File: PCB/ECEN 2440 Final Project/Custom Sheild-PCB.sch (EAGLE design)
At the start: 4 parts

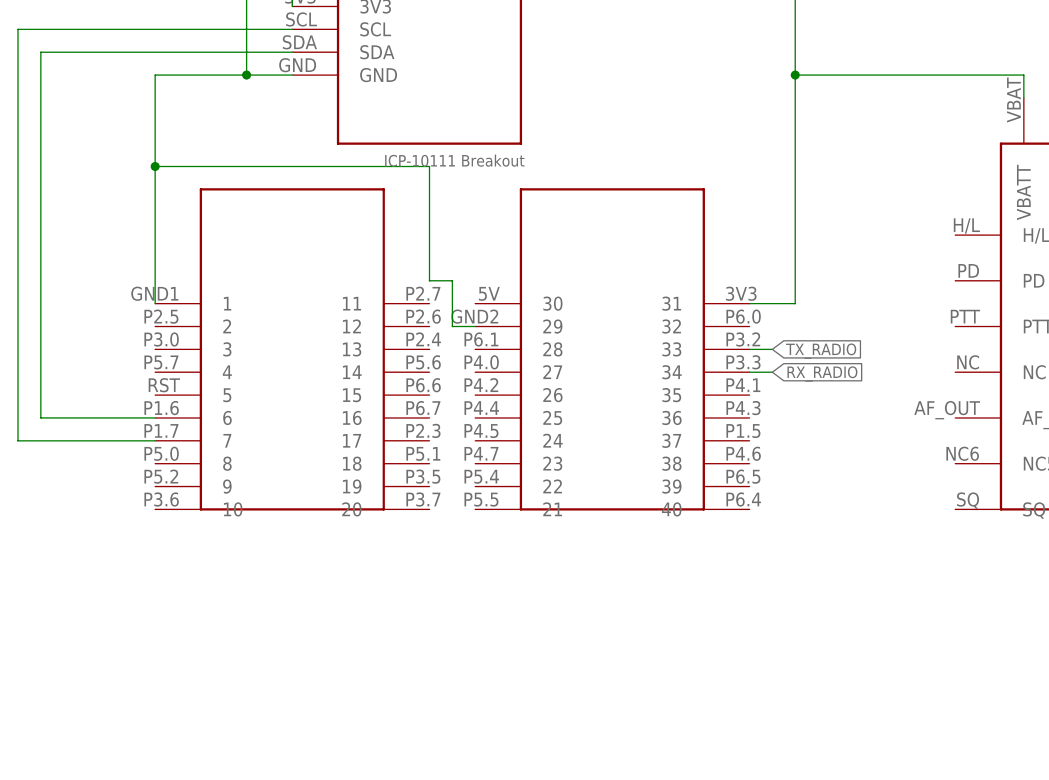
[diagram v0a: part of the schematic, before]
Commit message: made a couple connections
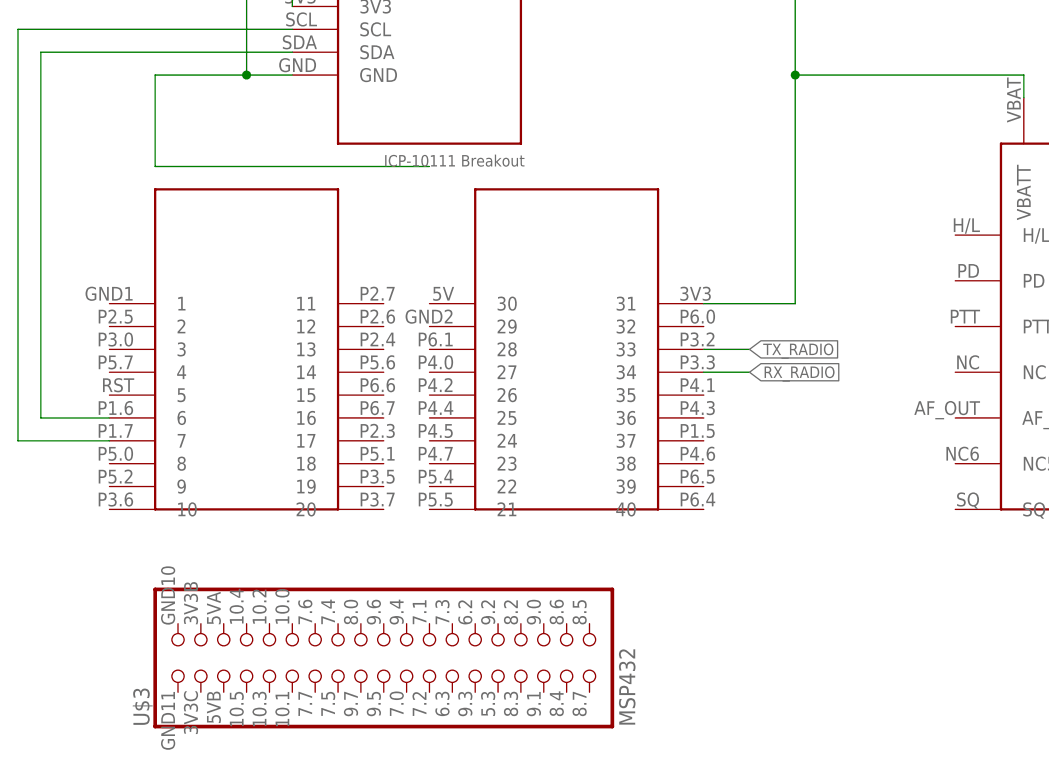
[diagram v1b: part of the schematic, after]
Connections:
- net GND1: no longer U$3.1, U$3.29
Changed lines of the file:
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@@
 <part name="U$1" library="adafruit" library_urn="urn:adsk.eagle:library:420" deviceset="MICROSD" device="" package3d_urn="urn:adsk.eagle:package:6240723/1"/>
 <part name="U$2" library="Custom Library" deviceset="ALTIMETER" device=""/>
+<part name="U$4" library="Custom Library" deviceset="RADIO" device=""/>
 <part name="U$3" library="Custom Library" deviceset="MSP432" device=""/>
-<part name="U$4" library="Custom Library" deviceset="RADIO" device=""/>
 </parts>
 <sheets>
@@
 <attribute name="NAME" x="76.2" y="60.96" size="1.27" layer="95" rot="R180"/>
 </instance>
-<instance part="U$3" gate="MSP432" x="50.8" y="27.94" smashed="yes"/>
 <instance part="U$4" gate="G$1" x="129.54" y="0" smashed="yes"/>
+<instance part="U$3" gate="MSP432" x="45.72" y="27.94" smashed="yes">
+<attribute name="NAME" x="34.925" y="-24.13" size="1.778" layer="95" rot="R90"/>
+<attribute name="VALUE" x="88.9" y="-24.13" size="1.778" layer="96" rot="R90"/>
+</instance>
 </instances>
 <busses>
@@
 <net name="GND1" class="0">
 <segment>
-<pinref part="U$3" gate="MSP432" pin="1"/>
 <pinref part="U$2" gate="G$1" pin="GND"/>
-<wire x1="35.56" y1="22.86" x2="35.56" y2="38.1" width="0.1524" layer="91"/>
 <wire x1="35.56" y1="38.1" x2="35.56" y2="48.26" width="0.1524" layer="91"/>
 <wire x1="35.56" y1="48.26" x2="45.72" y2="48.26" width="0.1524" layer="91"/>
 <wire x1="45.72" y1="48.26" x2="50.8" y2="48.26" width="0.1524" layer="91"/>
-<junction x="35.56" y="38.1"/>
 <wire x1="66.04" y1="38.1" x2="35.56" y2="38.1" width="0.1524" layer="91"/>
 <wire x1="45.72" y1="73.66" x2="45.72" y2="63.5" width="0.1524" layer="91"/>
@@
 <junction x="142.24" y="45.72"/>
 <junction x="45.72" y="63.5"/>
-<wire x1="66.04" y1="38.1" x2="66.04" y2="25.4" width="0.1524" layer="91"/>
-<wire x1="66.04" y1="25.4" x2="68.58" y2="25.4" width="0.1524" layer="91"/>
-<wire x1="68.58" y1="25.4" x2="68.58" y2="20.32" width="0.1524" layer="91"/>
-<pinref part="U$3" gate="MSP432" pin="29"/>
-<wire x1="68.58" y1="20.32" x2="71.12" y2="20.32" width="0.1524" layer="91"/>
 </segment>
 </net>
 <net name="N$1" class="0">
 <segment>
-<pinref part="U$3" gate="MSP432" pin="6"/>
-<wire x1="35.56" y1="10.16" x2="22.86" y2="10.16" width="0.1524" layer="91"/>
 <pinref part="U$2" gate="G$1" pin="SDA"/>
 <wire x1="22.86" y1="10.16" x2="22.86" y2="50.8" width="0.1524" layer="91"/>
 <wire x1="22.86" y1="50.8" x2="50.8" y2="50.8" width="0.1524" layer="91"/>
+<pinref part="U$3" gate="MSP432" pin="6"/>
+<wire x1="22.86" y1="10.16" x2="30.48" y2="10.16" width="0.1524" layer="91"/>
 </segment>
 </net>
 <net name="N$2" class="0">
 <segment>
-<pinref part="U$3" gate="MSP432" pin="7"/>
-<wire x1="35.56" y1="7.62" x2="20.32" y2="7.62" width="0.1524" layer="91"/>
 <pinref part="U$2" gate="G$1" pin="SCL"/>
 <wire x1="20.32" y1="7.62" x2="20.32" y2="53.34" width="0.1524" layer="91"/>
 <wire x1="20.32" y1="53.34" x2="50.8" y2="53.34" width="0.1524" layer="91"/>
+<pinref part="U$3" gate="MSP432" pin="7"/>
+<wire x1="20.32" y1="7.62" x2="30.48" y2="7.62" width="0.1524" layer="91"/>
 </segment>
 </net>
 <net name="N$3" class="0">
 <segment>
-<pinref part="U$3" gate="MSP432" pin="31"/>
-<wire x1="101.6" y1="22.86" x2="106.68" y2="22.86" width="0.1524" layer="91"/>
 <wire x1="106.68" y1="22.86" x2="106.68" y2="48.26" width="0.1524" layer="91"/>
 <wire x1="106.68" y1="48.26" x2="132.08" y2="48.26" width="0.1524" layer="91"/>
@@
 <wire x1="106.68" y1="60.96" x2="106.68" y2="48.26" width="0.1524" layer="91"/>
 <junction x="106.68" y="48.26"/>
+<pinref part="U$3" gate="MSP432" pin="31"/>
+<wire x1="106.68" y1="22.86" x2="96.52" y2="22.86" width="0.1524" layer="91"/>
 </segment>
 </net>
@@
 <segment>
 <pinref part="U$3" gate="MSP432" pin="34"/>
-<wire x1="101.6" y1="15.24" x2="104.14" y2="15.24" width="0.1524" layer="91"/>
-<label x="104.14" y="15.24" size="1.27" layer="95" xref="yes"/>
+<wire x1="96.52" y1="15.24" x2="101.6" y2="15.24" width="0.1524" layer="91"/>
+<label x="101.6" y="15.24" size="1.27" layer="95" xref="yes"/>
 </segment>
 </net>
@@
 <segment>
 <pinref part="U$3" gate="MSP432" pin="33"/>
-<wire x1="101.6" y1="17.78" x2="104.14" y2="17.78" width="0.1524" layer="91"/>
-<label x="104.14" y="17.78" size="1.27" layer="95" xref="yes"/>
+<wire x1="96.52" y1="17.78" x2="101.6" y2="17.78" width="0.1524" layer="91"/>
+<label x="101.6" y="17.78" size="1.27" layer="95" xref="yes"/>
 </segment>
 </net>

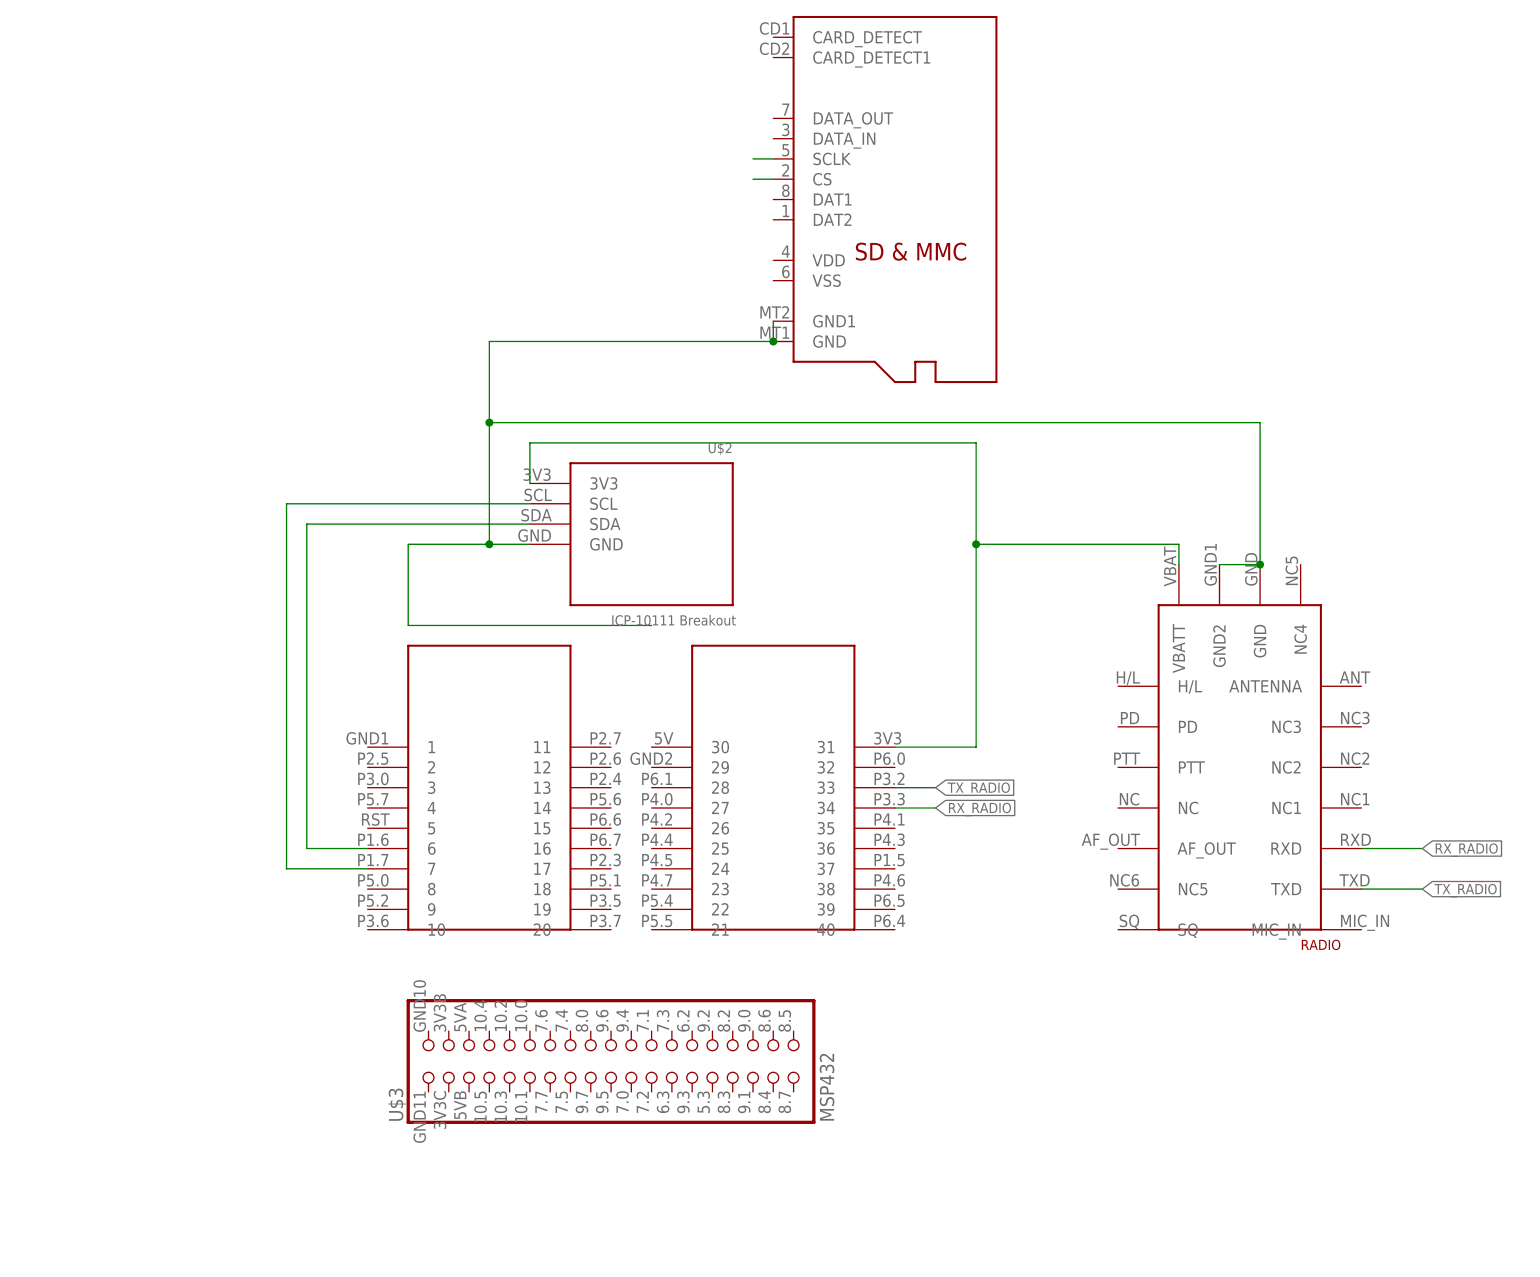
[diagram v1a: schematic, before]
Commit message: Connected Pins
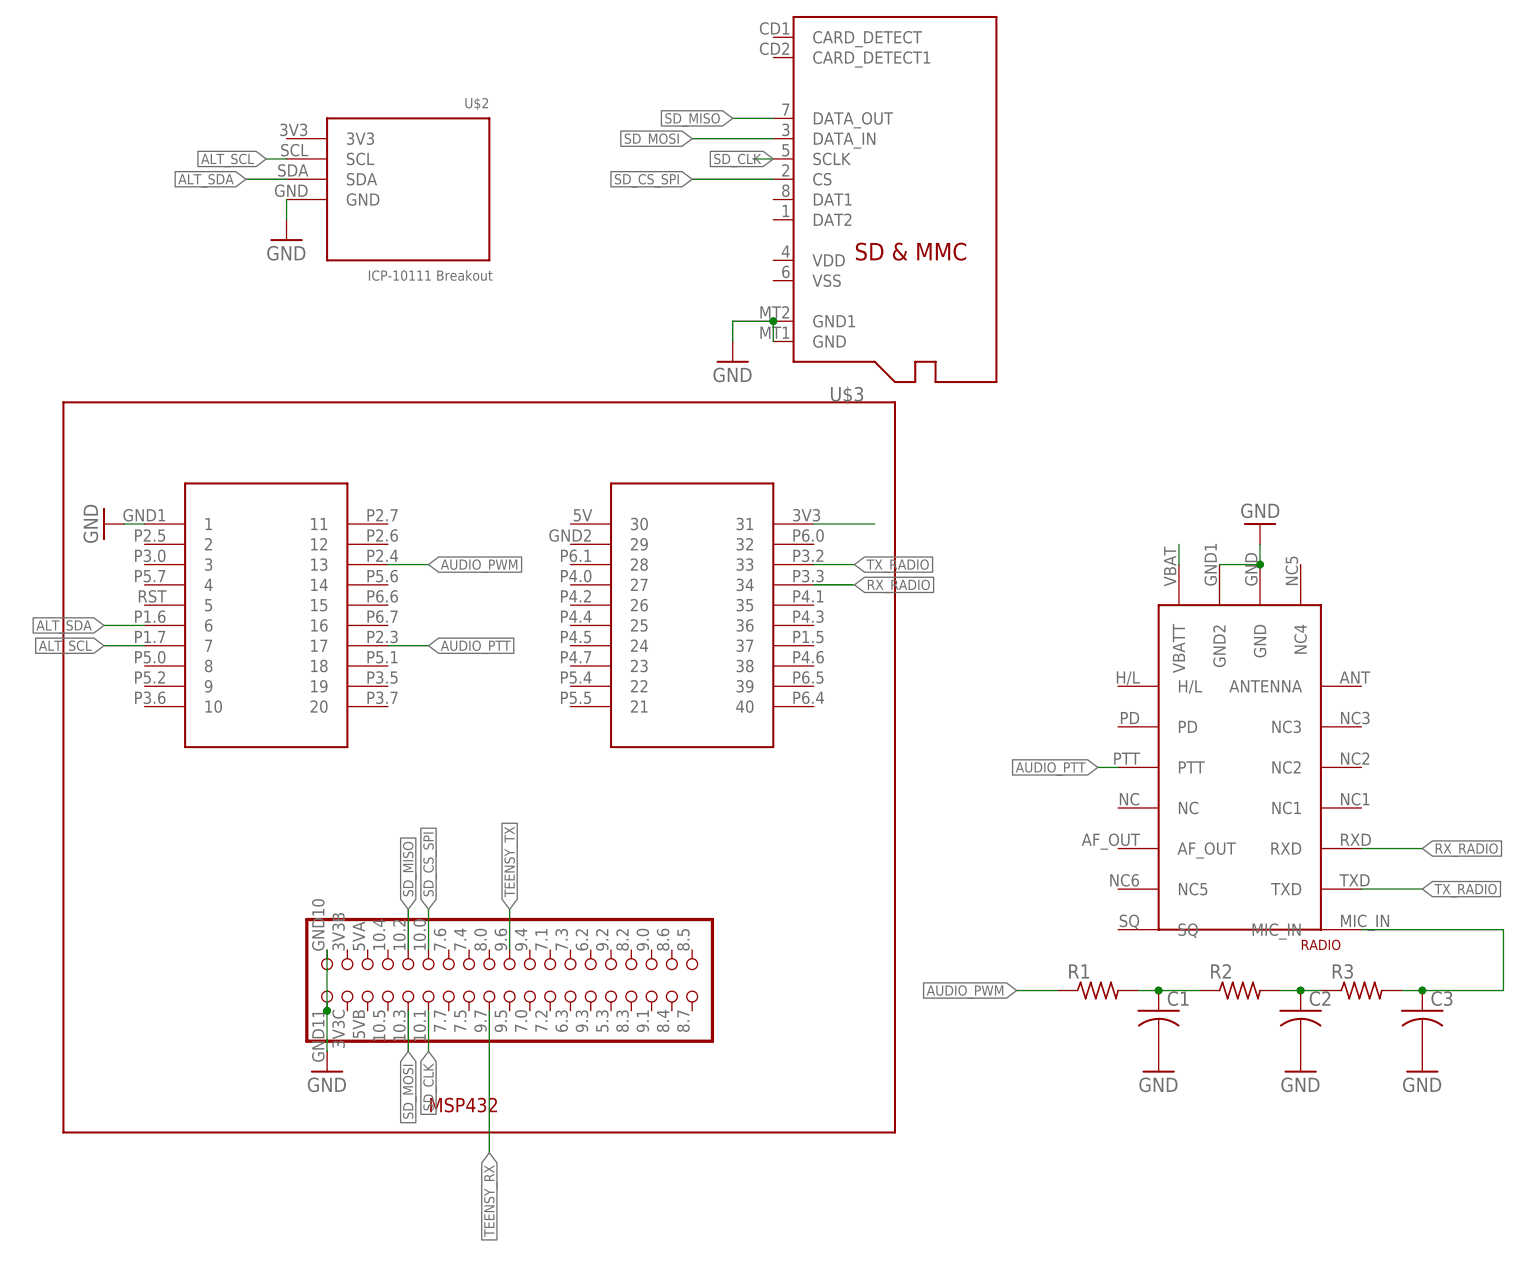
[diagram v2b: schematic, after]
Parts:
- added C1, C2, C3: (no value), rcl:C-USC0805
- added R1, R2, R3: (no value), rcl:R-US_R0805
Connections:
- net N$1 renamed ALT_SDA
- net N$2 renamed ALT_SCL
- removed net GND1: U$1.GND, U$1.GND1, U$2.GND, U$4.GND, U$4.GND2
- new net AUDIO_PTT: U$3.17, U$4.PTT
- new net AUDIO_PWM: R1.1, U$3.13
- new net GND: C1.2, C2.2, C3.2, U$1.GND, U$1.GND1, U$2.GND, U$3.1, U$3.41, U$3.42, U$4.GND, U$4.GND2
- new net N$1: U$3.31
- new net N$2: C1.1, R1.2, R2.1
- new net SD_CLK: U$1.SCLK, U$3.51
- new net SD_CS_SPI: U$1.CS, U$3.52
- new net SD_MISO: U$1.DATA_OUT, U$3.50
- new net SD_MOSI: U$1.DATA_IN, U$3.49
- new net TEENSY_RX: U$3.57
- new net TEENSY_TX: U$3.60
- net N$3: no longer U$2.3V3, U$3.31
- net N$4: now also C2.1, R2.2, R3.1; no longer U$1.CS
- net N$5: now also C3.1, R3.2, U$4.MIC_IN; no longer U$1.SCLK
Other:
- moved on the sheet: U$2
